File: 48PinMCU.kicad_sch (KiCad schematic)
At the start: 34 parts, among them J10 SWD, J9 SWD_Header, SW1 Reset, SW2 SW_SPDT, U8 STM32G473CETx, Y1 Crystal

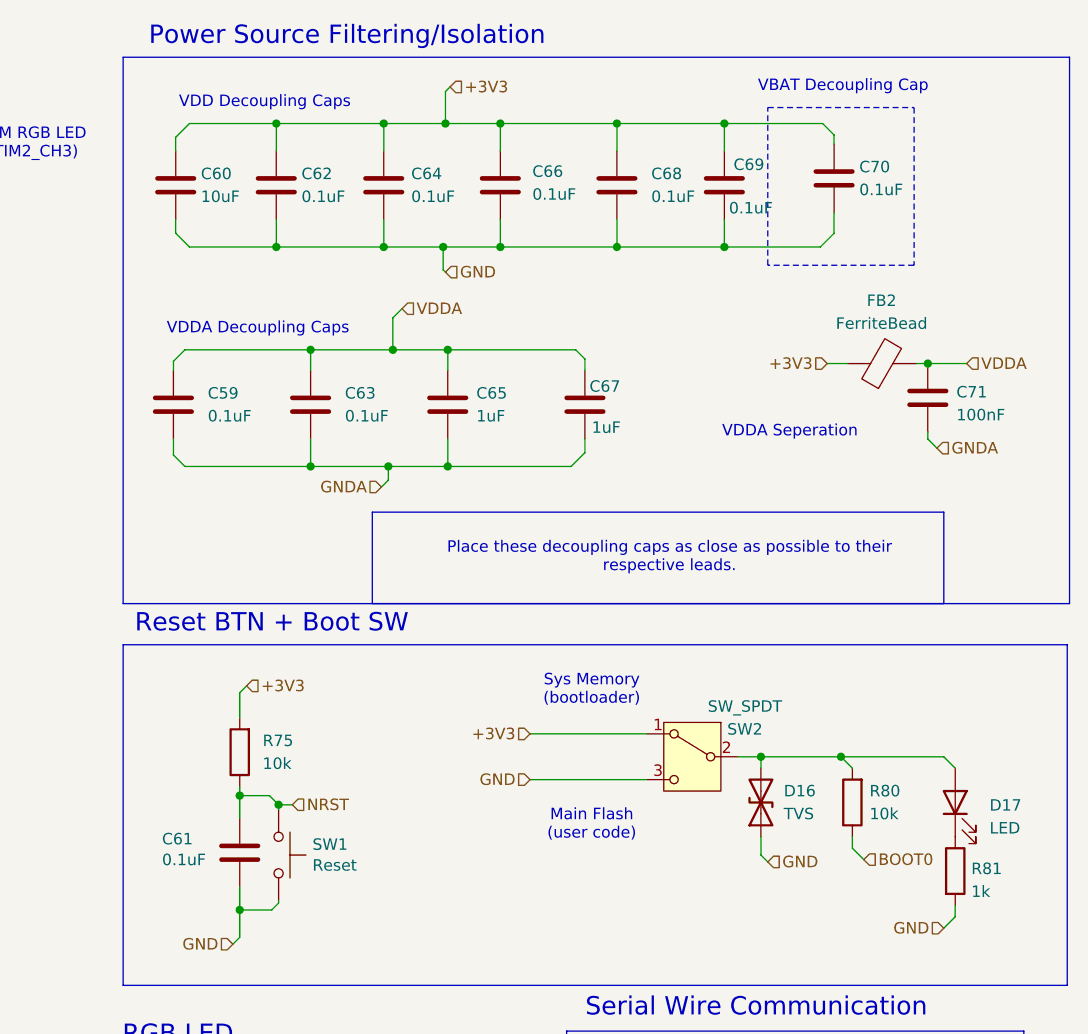
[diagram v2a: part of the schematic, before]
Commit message: footprints & schematic cute-ification
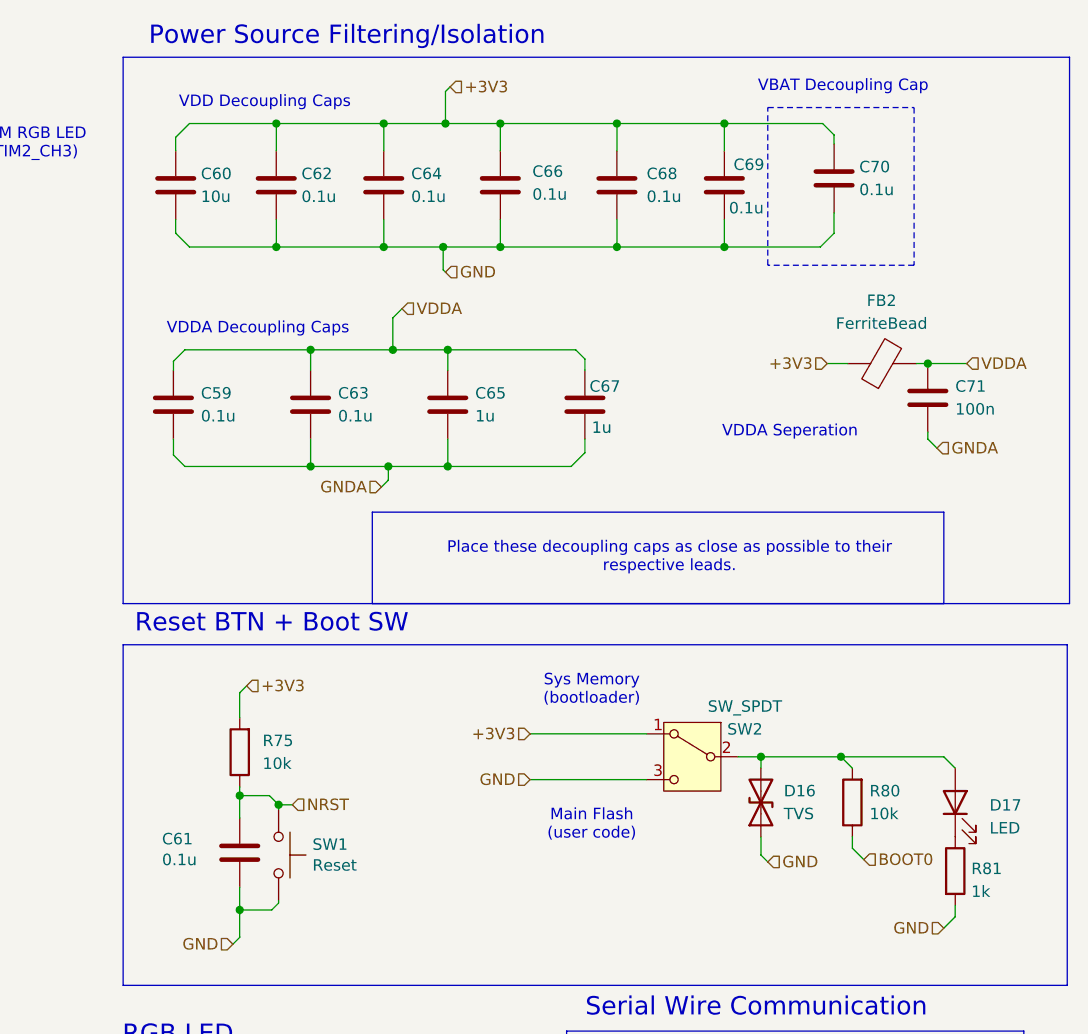
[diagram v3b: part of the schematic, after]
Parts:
- C59, C61, C62, C63, C64, C66, C68, C69, C70: value 0.1uF -> 0.1u
- C60: value 10uF -> 10u
- C65, C67: value 1uF -> 1u
- C71: value 100nF -> 100n
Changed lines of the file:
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@@
 		(fields_autoplaced yes)
 		(property "Reference" "C65"
-			(at 204.597 57.4039 0)
+			(at 204.47 57.4039 0)
 			(show_name no)
 			(do_not_autoplace no)
@@
 			)
 		)
-		(property "Value" "1uF"
-			(at 204.597 59.9439 0)
+		(property "Value" "1u"
+			(at 204.47 59.9439 0)
 			(show_name no)
 			(do_not_autoplace no)
@@
 			)
 		)
-		(property "Value" "0.1uF"
+		(property "Value" "0.1u"
 			(at 247.142 34.798 0)
 			(show_name no)
@@
 		(fields_autoplaced yes)
 		(property "Reference" "C63"
-			(at 189.992 57.4039 0)
+			(at 189.23 57.4039 0)
 			(show_name no)
 			(do_not_autoplace no)
@@
 			)
 		)
-		(property "Value" "0.1uF"
-			(at 189.992 59.9439 0)
+		(property "Value" "0.1u"
+			(at 189.23 59.9439 0)
 			(show_name no)
 			(do_not_autoplace no)
@@
 			)
 		)
-		(property "Value" "0.1uF"
+		(property "Value" "0.1u"
 			(at 185.166 35.56 0)
 			(show_name no)
@@
 		(fields_autoplaced yes)
 		(property "Reference" "C59"
-			(at 174.752 57.4039 0)
+			(at 173.99 57.4039 0)
 			(show_name no)
 			(do_not_autoplace no)
@@
 			)
 		)
-		(property "Value" "0.1uF"
-			(at 174.752 59.9439 0)
+		(property "Value" "0.1u"
+			(at 173.99 59.9439 0)
 			(show_name no)
 			(do_not_autoplace no)
@@
 		(fields_autoplaced yes)
 		(property "Reference" "C71"
-			(at 257.937 57.277 0)
+			(at 257.81 56.6419 0)
 			(show_name no)
 			(do_not_autoplace no)
@@
 			)
 		)
-		(property "Value" "100nF"
-			(at 257.937 59.817 0)
+		(property "Value" "100n"
+			(at 257.81 59.1819 0)
 			(show_name no)
 			(do_not_autoplace no)
@@
 			)
 		)
-		(property "Value" "0.1uF"
+		(property "Value" "0.1u"
 			(at 210.82 35.306 0)
 			(show_name no)
@@
 		(fields_autoplaced yes)
 		(property "Reference" "C68"
-			(at 224.028 33.0199 0)
+			(at 223.52 33.0199 0)
 			(show_name no)
 			(do_not_autoplace no)
@@
 			)
 		)
-		(property "Value" "0.1uF"
-			(at 224.028 35.5599 0)
+		(property "Value" "0.1u"
+			(at 223.52 35.5599 0)
 			(show_name no)
 			(do_not_autoplace no)
@@
 			)
 		)
-		(property "Value" "10uF"
+		(property "Value" "10u"
 			(at 173.99 35.56 0)
 			(show_name no)
@@
 			)
 		)
-		(property "Value" "1uF"
+		(property "Value" "1u"
 			(at 217.424 61.214 0)
 			(show_name no)
@@
 			)
 		)
-		(property "Value" "0.1uF"
+		(property "Value" "0.1u"
 			(at 169.672 109.2454 0)
 			(show_name no)
@@
 			)
 		)
-		(property "Value" "0.1uF"
+		(property "Value" "0.1u"
 			(at 197.358 35.56 0)
 			(show_name no)
@@
 			)
 		)
-		(property "Value" "0.1uF"
+		(property "Value" "0.1u"
 			(at 232.664 36.83 0)
 			(show_name no)
